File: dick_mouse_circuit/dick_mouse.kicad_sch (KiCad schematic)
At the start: 58 parts, among them J1 USB_C_Receptacle_USB2.0_16P, J10 Conn_01x04, J11 Conn_01x09, J2 AudioJack3, J3 Conn_01x03, J4 Conn_01x03, J5 Conn_01x03, J6 Conn_01x02, J7 Conn_01x02, J8 Conn_01x05, J9 Conn_01x05, SW1 SW_Push, SW2 SW_Push, SW3 SW_Push, SW4 SW_Push, SW5 SW_Push, SW6 SW_Push, SW7 SW_Push, U1 USBLC6-2SC6, U2 ESP32-S3-WROOM-1, U3 NJM4558, U4 AMS1117-3.3, U5 PCM5102A, U6 LM2776

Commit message: ボルテージフォロワ追加
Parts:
- removed C18: 2.2u, symbol Device:C
- added C17, C19: 2.2u, symbol Device:C
- R2, R3: value 10k -> 470
- renumbered C17 to C18, C19 to C20
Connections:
- net +5V: now also C17.1
- net GND: now also C17.2
- net CAPM: no longer names the net of U5.4 (CAPM)
- net CAPM: now also C19.2
- net CAPP: no longer names the net of U5.2 (CAPP)
- net CAPP: now also C19.1

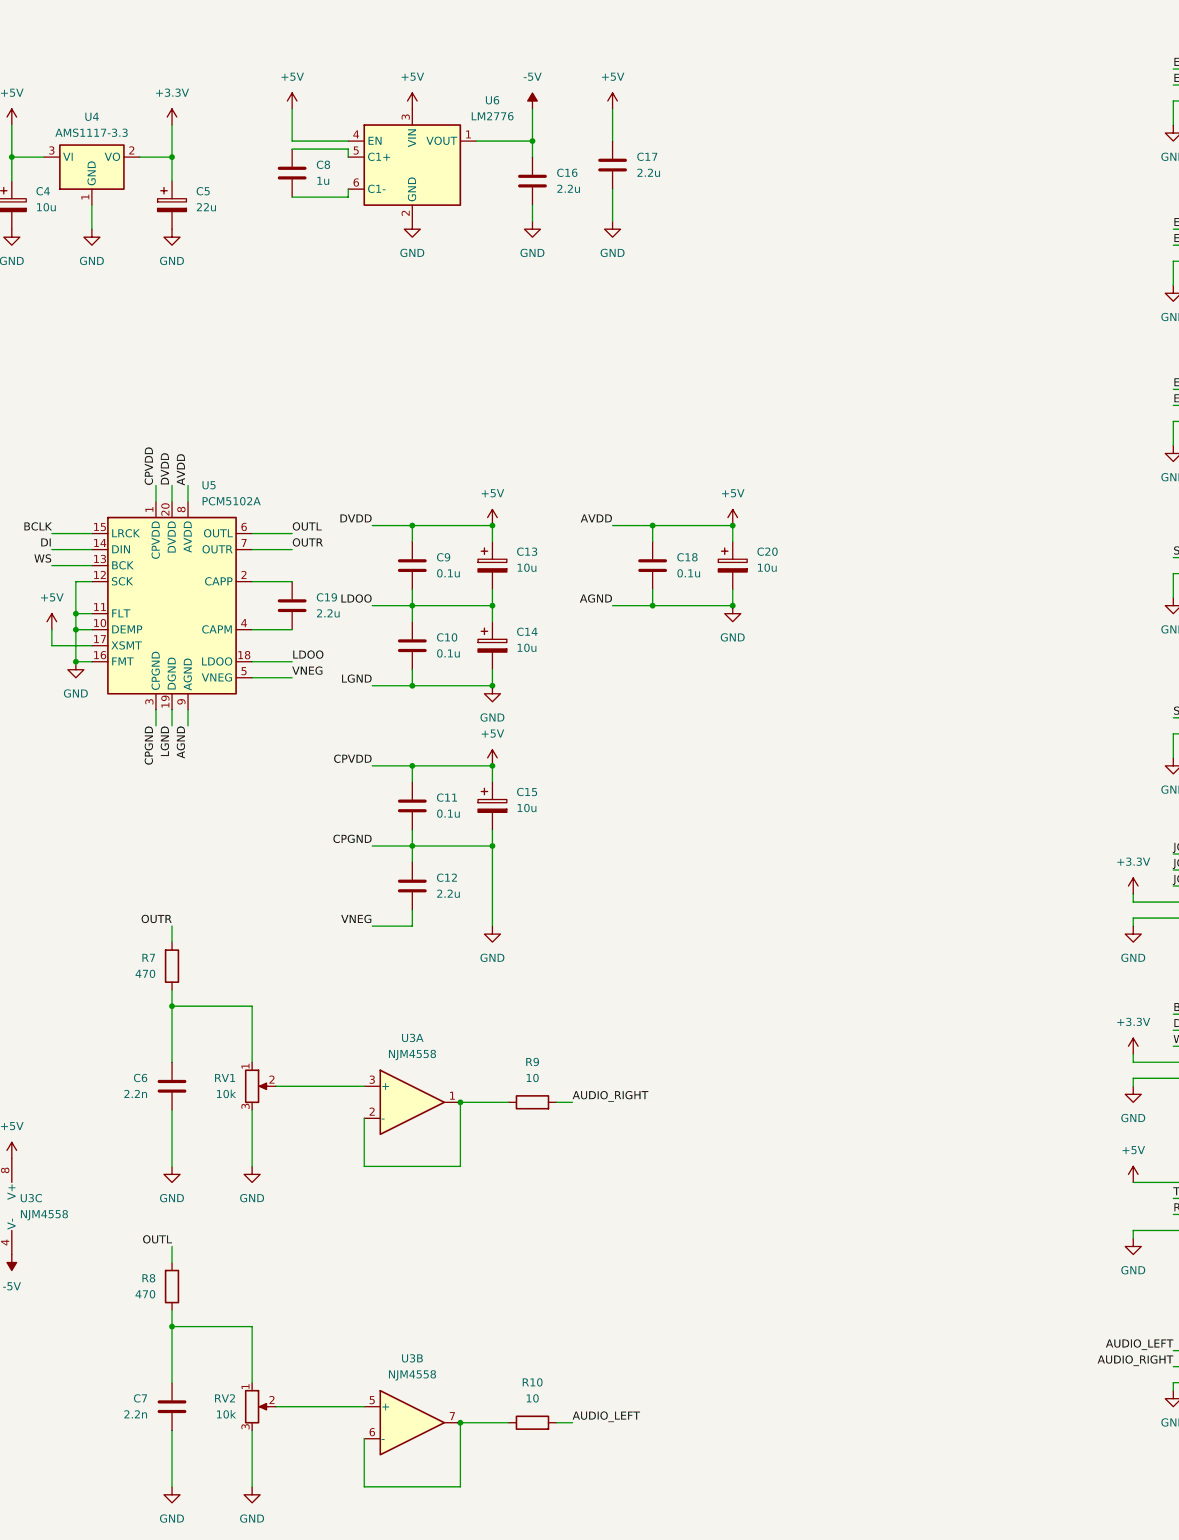
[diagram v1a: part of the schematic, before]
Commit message: オーディオ出力確認。オーディオ入力はWebRTCとpavucontrolで失敗。pw-recordで成功
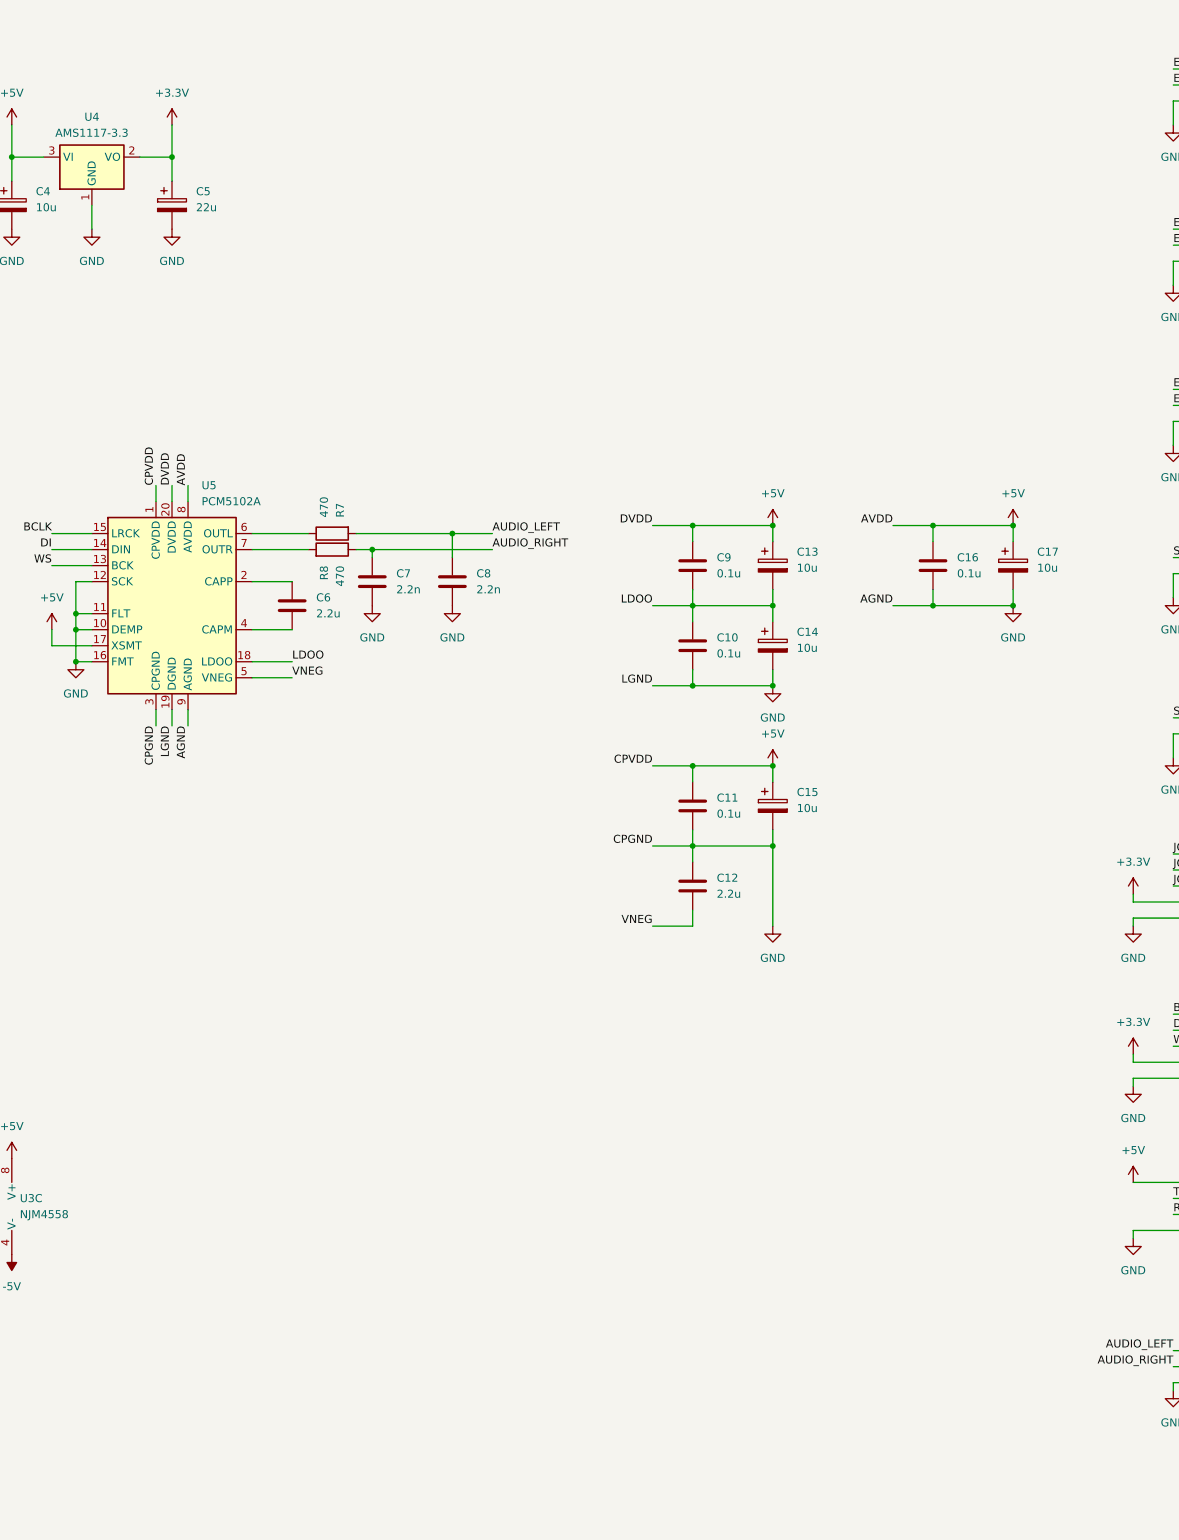
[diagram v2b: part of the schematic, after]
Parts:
- removed C16, C17: 2.2u, symbol Device:C
- removed C6: 2.2n, symbol Device:C
- removed C8: 1u, symbol Device:C
- removed R10, R9: 10, symbol Device:R
- removed RV1, RV2: 10k, symbol Device:R_Potentiometer
- removed unit 1 of U3
- removed unit 2 of U3
- removed U6: LM2776, Package_TO_SOT_SMD:SOT-23-6, symbol Regulator_SwitchedCapacitor:LM2776
- added C7: 2.2n, symbol Device:C
- renumbered C18 to C16, C20 to C17, C19 to C6, C7 to C8
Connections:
- net AUDIO_LEFT: now also C8.1, R7.2
- net AUDIO_RIGHT: now also R8.1, C7.1
- net GND: now also C7.2
- net at R7.1: now also U5.6 (OUTL)
- net OUTL: no longer names the net of R8.2
- net OUTL: now also U5.7 (OUTR); no longer U5.6 (OUTL)
- removed net OUTR: R7.2, U5.7 (OUTR)
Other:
- moved on the sheet: C10, C11, C12, C13, C14, C15, C16, C17, C8, C9, R8
